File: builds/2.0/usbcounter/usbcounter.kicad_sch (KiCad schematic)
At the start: 38 parts, among them IC1 ATTINY826-XUR, J1 UJ2-MIBH-G-SMT-TR, J2 Conn_IN, J3 Conn_Prog, J4 Conn_Disp, U1 MCP23008-xSO, U2 FT230XS, U3 74LV8154, U4 MCP23008-xSO, U5 NCP1117 3.3V, Y1 14.7456 MHz TCXO

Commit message: 2.0: ready to fabricate
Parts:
- J3, J4: footprint Resistor_SMD:R_0805_2012Metric_Pad1.20x1.40mm_HandSolder -> Connector_PinHeader_2.54mm:PinHeader_1x05_P2.54mm_Vertical
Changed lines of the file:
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@@
   (symbol (lib_id "power:PWR_FLAG") (at 57.15 24.13 0) (unit 1)
     (in_bom yes) (on_board yes)
-    (property "Reference" "#FLG0102" (id 0) (at 57.15 22.225 0)
+    (property "Reference" "#FLG01" (id 0) (at 57.15 22.225 0)
       (effects (font (size 1.27 1.27)) hide)
     )
@@
     (pin "2")
   )
+  (symbol (lib_id "Graphic:Logo_Open_Hardware_Small") (at 213.36 149.225 0) (unit 1)
+    (in_bom yes) (on_board yes) (fields_autoplaced)
+    (property "Reference" "#LOGO1" (id 0) (at 213.36 142.24 0))
+    (property "Value" "Logo_Open_Hardware_Small" (id 1) (at 213.36 154.94 0))
+    (property "Footprint" "" (id 2) (at 213.36 149.225 0)
+      (effects (font (size 1.27 1.27)) hide)
+    )
+    (property "Datasheet" "~" (id 3) (at 213.36 149.225 0)
+      (effects (font (size 1.27 1.27)) hide)
+    )
+  )
   (symbol (lib_id "power:GND") (at 35.56 134.62 270) (unit 1)
     (in_bom yes) (on_board yes)
@@
     (property "Reference" "J3" (id 0) (at 217.17 64.77 0))
     (property "Value" "Conn_Prog" (id 1) (at 220.98 67.31 0))
-    (property "Footprint" "Resistor_SMD:R_0805_2012Metric_Pad1.20x1.40mm_HandSolder" (id 2) (at 215.9 76.2 0)
+    (property "Footprint" "Connector_PinHeader_2.54mm:PinHeader_1x05_P2.54mm_Vertical" (id 2) (at 215.9 76.2 0)
       (effects (font (size 1.27 1.27)) hide)
     )
@@
     (property "Reference" "J4" (id 0) (at 246.38 64.77 0))
     (property "Value" "Conn_Disp" (id 1) (at 250.19 67.31 0))
-    (property "Footprint" "Resistor_SMD:R_0805_2012Metric_Pad1.20x1.40mm_HandSolder" (id 2) (at 246.38 76.2 0)
+    (property "Footprint" "Connector_PinHeader_2.54mm:PinHeader_1x05_P2.54mm_Vertical" (id 2) (at 246.38 76.2 0)
       (effects (font (size 1.27 1.27)) hide)
     )
@@
   (symbol (lib_id "power:PWR_FLAG") (at 220.98 31.75 0) (unit 1)
     (in_bom yes) (on_board yes)
-    (property "Reference" "#FLG01" (id 0) (at 220.98 29.845 0)
+    (property "Reference" "#FLG02" (id 0) (at 220.98 29.845 0)
       (effects (font (size 1.27 1.27)) hide)
     )
@@
   (symbol (lib_id "power:PWR_FLAG") (at 220.98 44.45 180) (unit 1)
     (in_bom yes) (on_board yes)
-    (property "Reference" "#FLG0101" (id 0) (at 220.98 46.355 0)
+    (property "Reference" "#FLG03" (id 0) (at 220.98 46.355 0)
       (effects (font (size 1.27 1.27)) hide)
     )
@@
   )
   (symbol_instances
+    (path "/62078469-6522-4cef-ad1e-2c608e1ebc46"
+      (reference "#FLG01") (unit 1) (value "PWR_FLAG") (footprint "")
+    )
     (path "/e2dcb0a8-f669-491c-8f92-e4c493b0292b"
-      (reference "#FLG01") (unit 1) (value "PWR_FLAG") (footprint "")
+      (reference "#FLG02") (unit 1) (value "PWR_FLAG") (footprint "")
     )
     (path "/f4ef4251-ecfc-4a05-ba74-f1e44e470a4a"
-      (reference "#FLG0101") (unit 1) (value "PWR_FLAG") (footprint "")
-    )
-    (path "/62078469-6522-4cef-ad1e-2c608e1ebc46"
-      (reference "#FLG0102") (unit 1) (value "PWR_FLAG") (footprint "")
+      (reference "#FLG03") (unit 1) (value "PWR_FLAG") (footprint "")
+    )
+    (path "/6d8d0b2a-4012-463f-915b-600d09459379"
+      (reference "#LOGO1") (unit 1) (value "Logo_Open_Hardware_Small") (footprint "")
     )
     (path "/fde752a2-cd3b-4b88-8bc2-d369736aebaa"
@@
     )
     (path "/9aabcf02-b49e-435c-91ec-c03af8d843a0"
-      (reference "J3") (unit 1) (value "Conn_Prog") (footprint "Resistor_SMD:R_0805_2012Metric_Pad1.20x1.40mm_HandSolder")
+      (reference "J3") (unit 1) (value "Conn_Prog") (footprint "Connector_PinHeader_2.54mm:PinHeader_1x05_P2.54mm_Vertical")
     )
     (path "/abdd414b-74de-4bbb-81cf-b169506a87d5"
-      (reference "J4") (unit 1) (value "Conn_Disp") (footprint "Resistor_SMD:R_0805_2012Metric_Pad1.20x1.40mm_HandSolder")
+      (reference "J4") (unit 1) (value "Conn_Disp") (footprint "Connector_PinHeader_2.54mm:PinHeader_1x05_P2.54mm_Vertical")
     )
     (path "/da46f722-1eae-416d-8dad-7ea491feaca1"

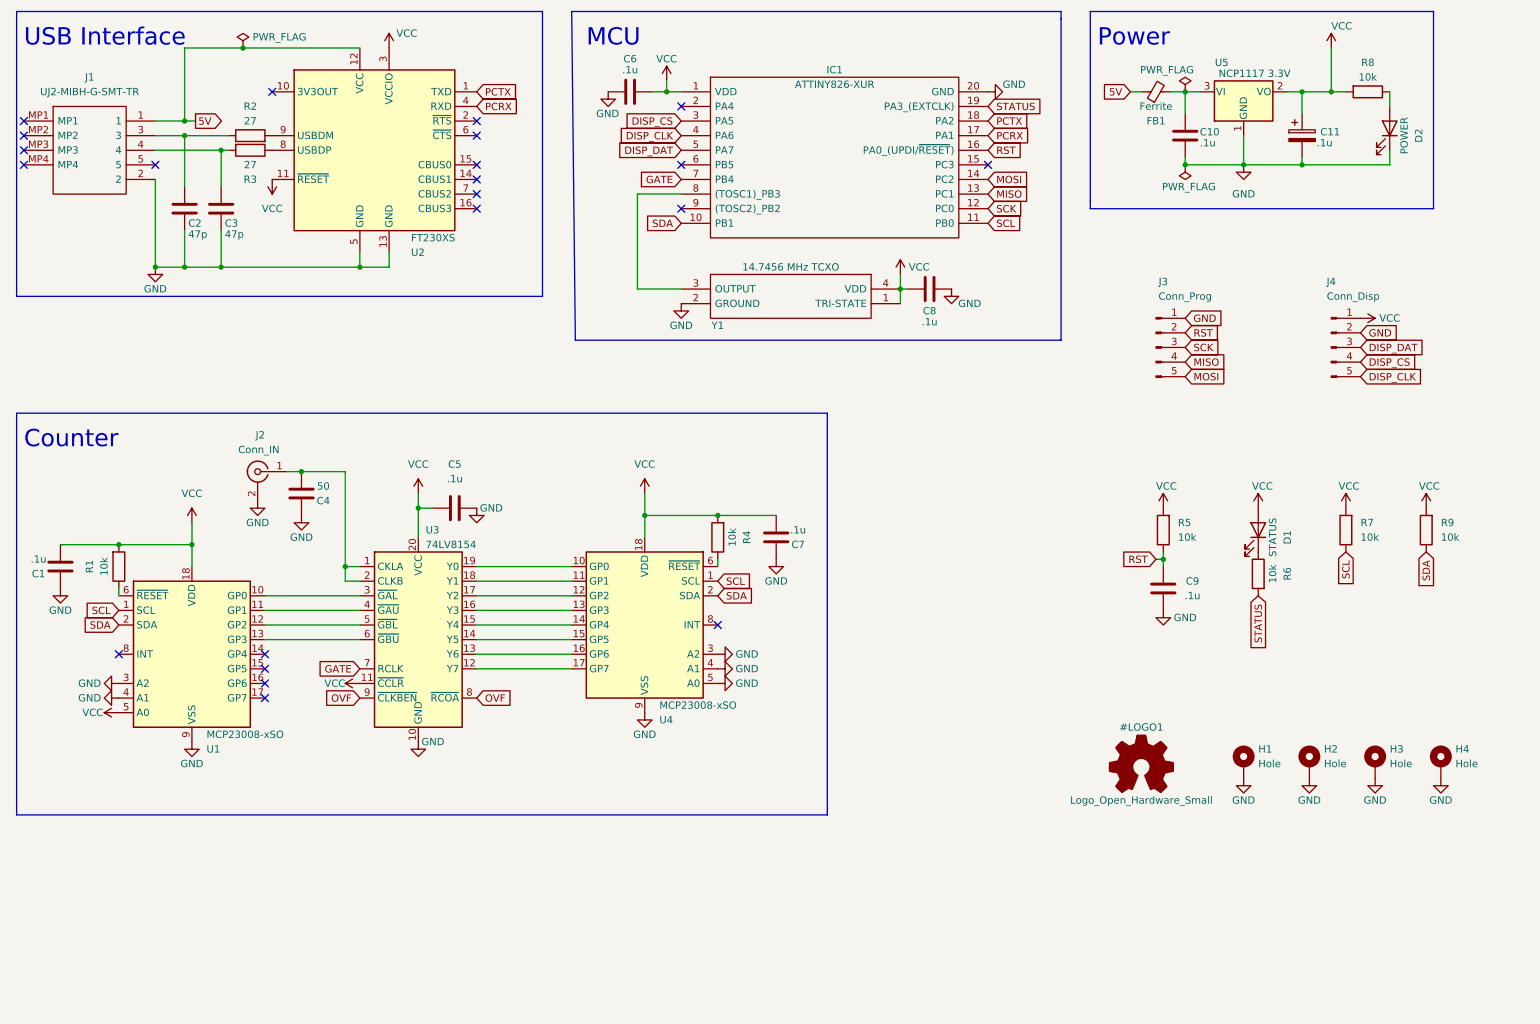
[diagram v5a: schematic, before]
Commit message: 3.0: update frontend
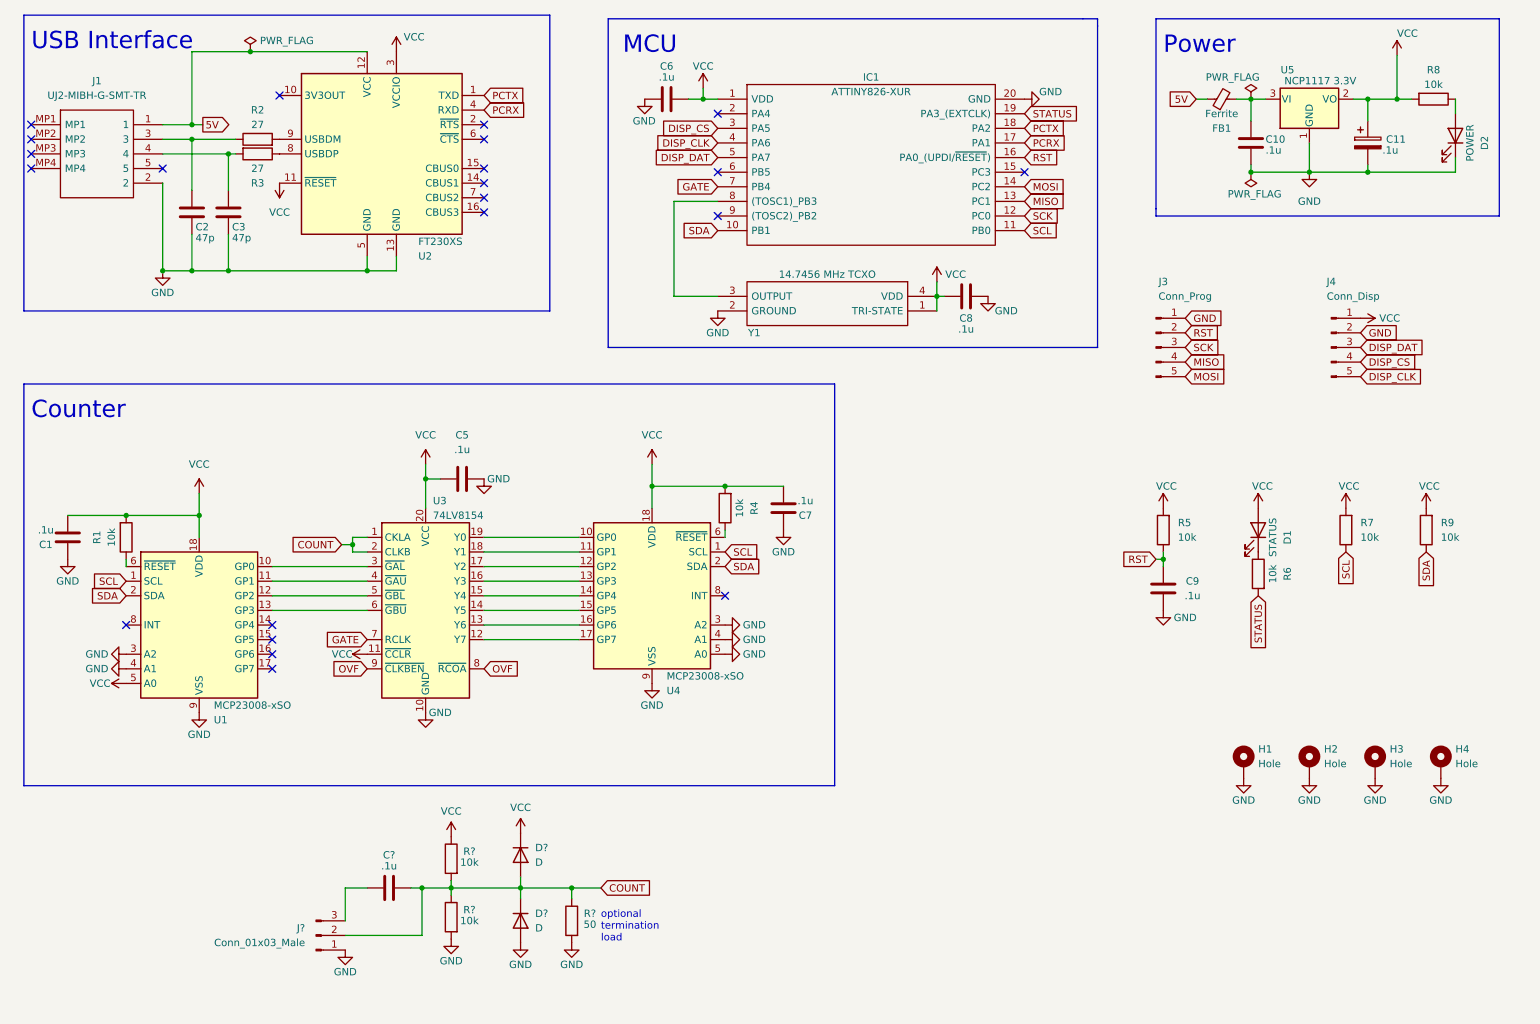
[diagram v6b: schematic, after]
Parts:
- removed C4: 50, Capacitor_SMD:C_0805_2012Metric_Pad1.18x1.45mm_HandSolder, symbol Device:C
- removed J2: Conn_IN, Connector_Coaxial:SMA_Amphenol_132291_Vertical, symbol Connector:Conn_Coaxial
- added C?: .1u, Capacitor_SMD:C_0805_2012Metric_Pad1.18x1.45mm_HandSolder, symbol Device:C
- added D? (x2): D, symbol Device:D
- added J?: Conn_01x03_Male, symbol Connector:Conn_01x03_Male
- added R? (x2): 10k, Resistor_SMD:R_0805_2012Metric_Pad1.20x1.40mm_HandSolder, symbol Device:R
- added R?: 50, Resistor_SMD:R_0805_2012Metric_Pad1.20x1.40mm_HandSolder, symbol Device:R
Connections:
- net GND: now also D?.2 (A), J?.1 (Pin_1), R?.2, R?.2
- net VCC: now also D?.1 (K), R?.1
- net COUNT: now reaches U3.1 (CKLA), U3.2 (CLKB)
- net COUNT: now also C?.1, D?.1 (K), D?.2 (A), J?.2 (Pin_2), R?.1, R?.1, R?.2
- new net: C?.2, J?.3 (Pin_3)
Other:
- note added: "optional termination load"
- moved on the sheet: C1, C10, C11, C2, C3, C5, C6, C7, C8, D2, FB1, IC1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

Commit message: 2.0: input protection and amplification
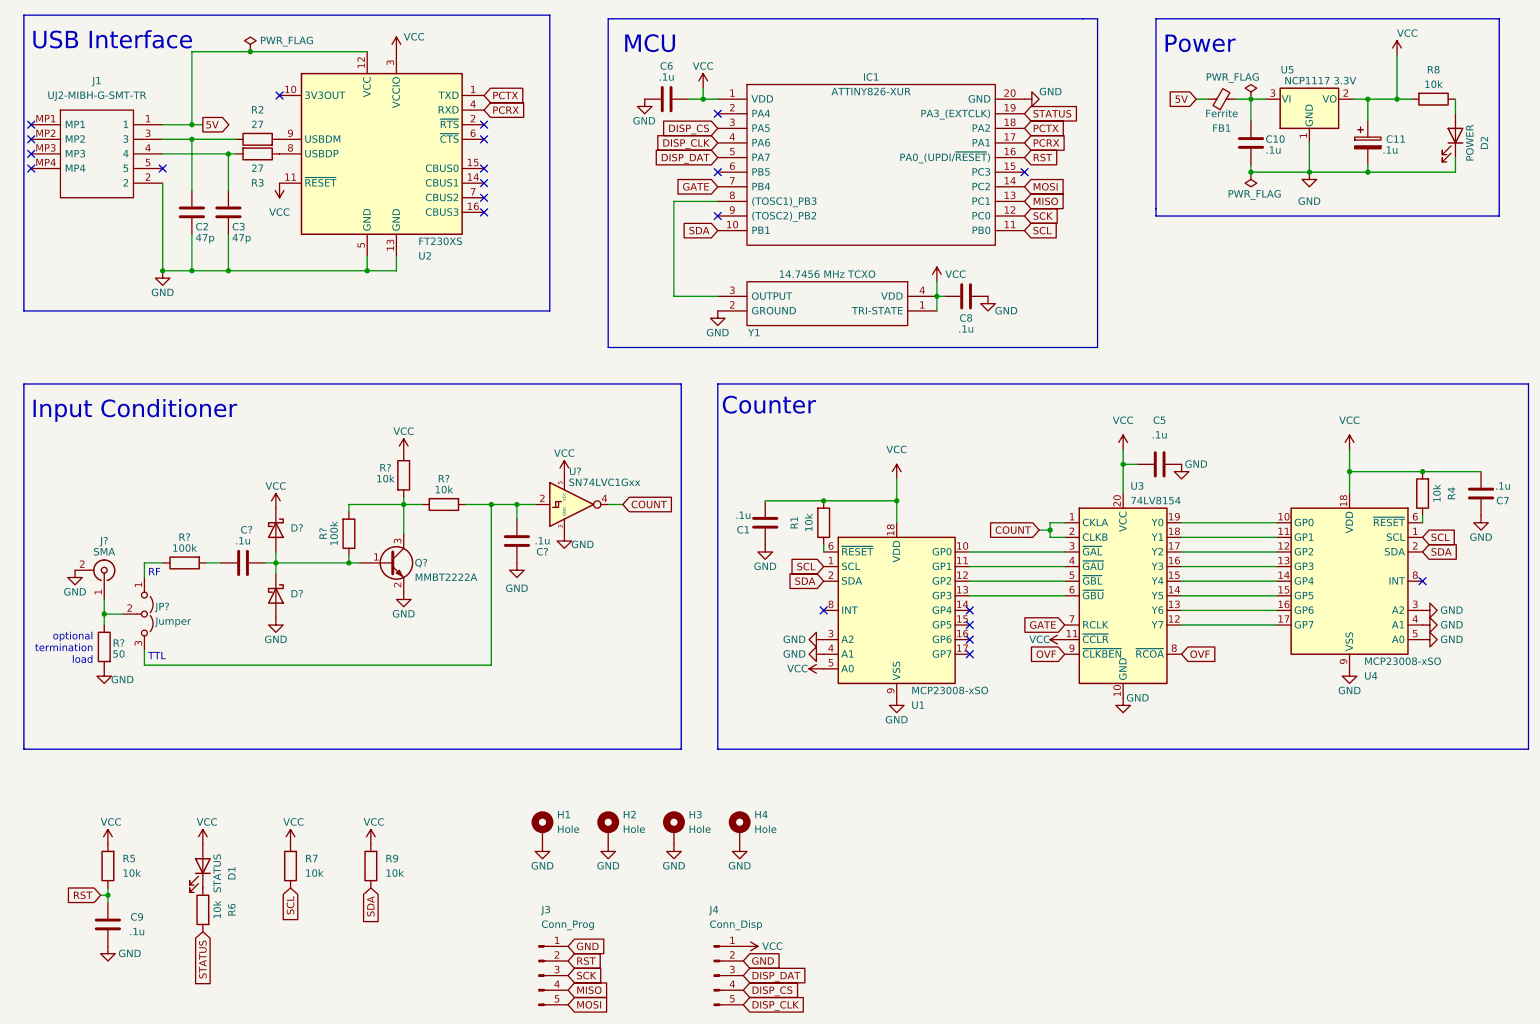
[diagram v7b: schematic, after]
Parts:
- removed C?: .1u, Capacitor_SMD:C_0805_2012Metric_Pad1.18x1.45mm_HandSolder, symbol Device:C
- removed D? (x2): D, symbol Device:D
- removed J?: Conn_01x03_Male, symbol Connector:Conn_01x03_Male
- removed R? (x2): 10k, Resistor_SMD:R_0805_2012Metric_Pad1.20x1.40mm_HandSolder, symbol Device:R
- removed R?: 50, Resistor_SMD:R_0805_2012Metric_Pad1.20x1.40mm_HandSolder, symbol Device:R
- added C? (x2): .1u, Capacitor_SMD:C_0805_2012Metric_Pad1.18x1.45mm_HandSolder, symbol Device:C
- added D? (x2): D, symbol Device:D_Schottky
- added J?: SMA, symbol Connector:Conn_Coaxial
- added JP?: Jumper, symbol Jumper:Jumper_3_Open
- added Q?: MMBT2222A, symbol Device:Q_NPN_BEC
- added R? (x2): 100k, Resistor_SMD:R_0805_2012Metric_Pad1.20x1.40mm_HandSolder, symbol Device:R
- added R? (x2): 10k, Resistor_SMD:R_0805_2012Metric_Pad1.20x1.40mm_HandSolder, symbol Device:R
- added R?: 50, Resistor_SMD:R_0805_2012Metric_Pad1.20x1.40mm_HandSolder, symbol Device:R
- added U?: SN74LVC1Gxx, Package_TO_SOT_SMD:SOT-23-5, symbol 74xGxx:SN74LVC1G14DBV
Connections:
- net COUNT: now also U?.4
- net GND: now also C?.1, D?.2 (A), J?.2 (Ext), Q?.2 (E), R?.2, U?.3 (GND)
- net VCC: now also D?.1 (K), R?.1, U?.5 (VCC)
- new net: JP?.1 (A), R?.1
- new net: C?.2, R?.2
- new net: C?.2, JP?.3 (B), R?.2, U?.2
- new net: Q?.3 (C), R?.1, R?.2, R?.2
- new net: J?.1 (In), JP?.2 (C), R?.1
- new net: C?.1, D?.1 (K), D?.2 (A), Q?.1 (B), R?.1
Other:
- note added: "Input Conditioner"
- note added: "RF"
- note added: "TTL"
- moved on the sheet: C1, C5, C7, C9, D1, H1, H2, H3, H4, J3, J4, R1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

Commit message: 2.0: update footprints
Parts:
- D2, D3: renamed from D?; footprint (none) -> Diode_SMD:D_SOD-323_HandSoldering
- J2: renamed from J?; footprint (none) -> Connector_Coaxial:SMA_Amphenol_901-144_Vertical
- JP1: renamed from JP?; footprint (none) -> Connector_PinHeader_2.54mm:PinHeader_1x03_P2.54mm_Vertical
- Q1: renamed from Q?; footprint (none) -> Package_TO_SOT_SMD:SOT-23
- gave numbers to parts that had none: 8
- renumbered C9 to C1, C7 to C12, C1 to C7, C5 to C9, D2 to D4, R1 to R12, R4 to R13, R8 to R14, R5 to R2, R6 to R4, R2 to R5, R3 to R6, U2 to U1, U1 to U3, U3 to U4, U4 to U6
